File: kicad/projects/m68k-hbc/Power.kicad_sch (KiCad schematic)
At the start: 25 parts, among them J16 ATX-24

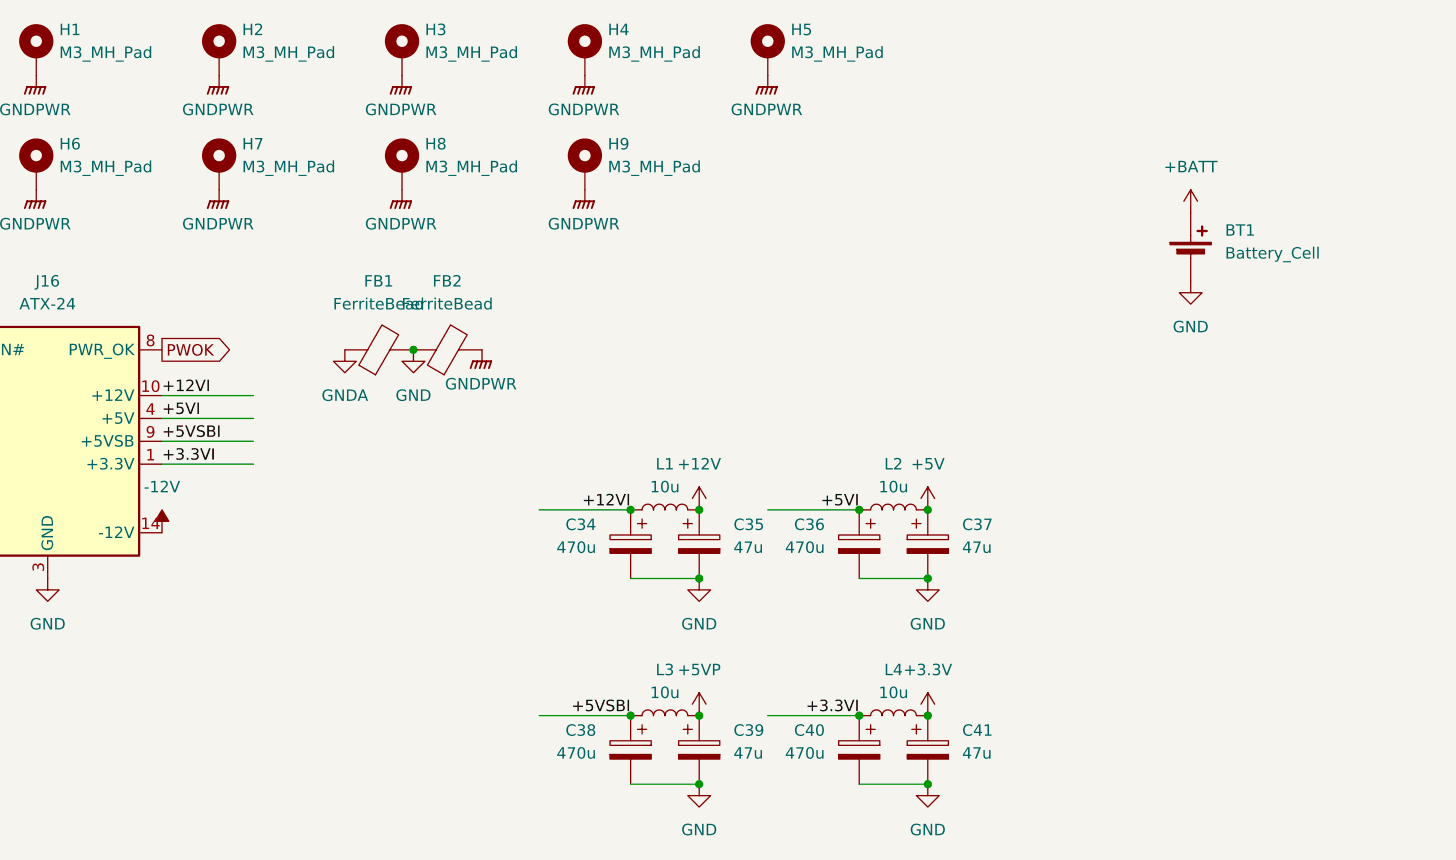
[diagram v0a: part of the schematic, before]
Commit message: Modified system architecture, New KiCad Project: Cache Memory Module(SIMM80)
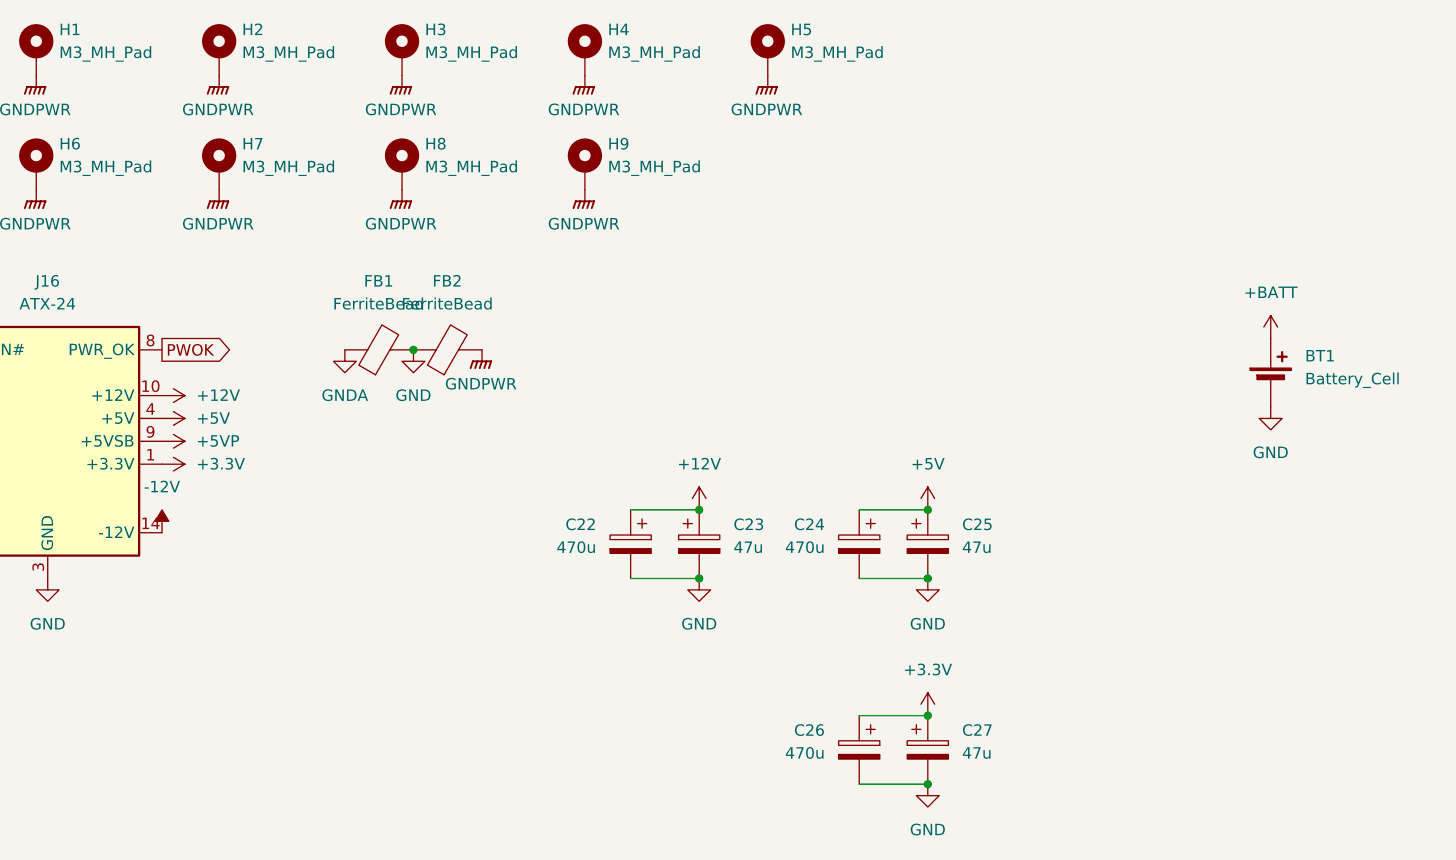
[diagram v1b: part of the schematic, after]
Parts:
- removed C38: 470u, Capacitor_THT:CP_Radial_D8.0mm_P3.50mm, symbol Device:C_Polarized
- removed C39: 47u, Capacitor_THT:CP_Radial_D8.0mm_P3.50mm, symbol Device:C_Polarized
- removed L1, L2, L3, L4: 10u, Inductor_THT:L_Toroid_Vertical_L13.0mm_W6.5mm_P5.60mm, symbol Device:L
- renumbered C34 to C22, C35 to C23, C36 to C24, C37 to C25, C40 to C26, C41 to C27
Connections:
- net +12VI is gone; now on net +12V: C22.1, J16.10 (+12V), J16.11 (+12V)
- net +3.3VI is gone; now on net +3.3V: C26.1, J16.1 (+3.3V), J16.12 (+3.3V), J16.13 (+3.3V), J16.2 (+3.3V)
- net +5VI is gone; now on net +5V: C24.1, J16.21 (+5V), J16.22 (+5V), J16.23 (+5V), J16.4 (+5V), J16.6 (+5V)
- net +5VSBI is gone; now on net +5VP: J16.9 (+5VSB)
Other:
- moved on the sheet: BT1

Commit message: Some Updates
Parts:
- added C132, C135, C136, C137, C138, C145, C146, C147, C148, C149, C150, C151, C154, C155, C156, C157, C158, C159, C160, C161, C162, C163, C164, C165: C, Capacitor_SMD:C_0603_1608Metric_Pad1.08x0.95mm_HandSolder, symbol Device:C
- added C133, C134, C143, C144: C_Polarized, Capacitor_THT:CP_Radial_D5.0mm_P2.50mm, symbol Device:C_Polarized
- added D2, D3, D4: D_Schottky, Diode_THT:D_5W_P12.70mm_Horizontal, symbol Device:D_Schottky
- added L8, L9: L, Inductor_SMD:L_10.4x10.4_H4.8, symbol Device:L
- added Q1, Q2: Q_PNP_BCE, RJK0651DPB-00:LFPAK_REN-M, symbol Device:Q_PNP_BCE
- added R40, R41, R42, R43, R44, R45, R46, R47, R48, R49, R50, R51, R52, R53, R54, R55, R56, R57, R58, R59, R60, R61, R62, R63: R, Resistor_SMD:R_0603_1608Metric_Pad0.98x0.95mm_HandSolder, symbol Device:R
- added RN5: R_Network08, Resistor_THT:R_Array_SIP9, symbol Device:R_Network08
- added U32: PAC1953x-x4MX, Package_DFN_QFN:VQFN-16-1EP_3x3mm_P0.5mm_EP1.1x1.1mm, symbol Sensor_Energy:PAC1953x-x4MX
- added U33, U34, U36, U37: RJK0651DPB-00-J5, LFPAK_REN, symbol RJK0651DPB-00:RJK0651DPB-00-J5
- added U35: LTC3886, Package_DFN_QFN:Linear_UGK52_QFN-46-52, symbol Regulator_Switching:LTC3886
- C139: renamed from C22; value 470u -> C_Polarized
- C140: renamed from C23; value 47u -> C_Polarized
- C141: renamed from C24; value 470u -> C_Polarized
- C142: renamed from C25; value 47u -> C_Polarized
- C152: renamed from C26; value 470u -> C_Polarized
- C153: renamed from C27; value 47u -> C_Polarized
- H1, H2, H3, H4, H5, H6, H7, H8, H9: value M3_MH_Pad -> MountingHole_Pad
- renumbered FB1 to FB2, FB2 to FB3
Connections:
- net +12V: now also C132.1, R40.2, R44.1, R45.1, U32.12 (SENSE1-), U33.5, U34.5, U35.47 (Iin+); no longer J16.10 (+12V), J16.11 (+12V)
- net +3.3V: now also R42.2, U32.7 (SENSE3-); no longer J16.1 (+3.3V), J16.12 (+3.3V), J16.13 (+3.3V), J16.2 (+3.3V)
- net +5V: now also R41.2, U32.14 (SENSE2-), U32.2 (V_{DD}); no longer J16.21 (+5V), J16.22 (+5V), J16.23 (+5V), J16.4 (+5V), J16.6 (+5V)
- net GND: now also C132.2, C133.2, C134.2, C135.2, C136.2, C137.2, C138.2, C143.2, C144.2, C145.2, C146.2, C147.2, C148.2, C149.1, C150.2, C151.2, C158.2, C159.2, C160.2, C161.2, C162.2, C163.2, C164.2, C165.2, D4.2 (A), Q1.1 (B), Q1.2 (C), Q2.1 (B), Q2.2 (C), R43.2, R58.2, R59.2, R60.2, R61.2, R62.2, U32.10 (GND), U32.17 (EP), U32.3 (GND), U32.9 (GND), U35.26 (PHAS_CFG), U35.28 (WP), U35.53 (GND), U35.8 (Vsense0-), U36.1, U36.2, U36.3, U37.1, U37.2, U37.3
- new net: C154.1, L8.2, U33.1, U33.2, U33.3, U35.1 (SW0), U36.5
- new net: C157.2, R51.1, U35.10 (Isense1-)
- new net: C160.1, U35.11 (Ithr0)
- new net: C161.1, U35.12 (Ith0)
- new net: U33.4, U35.2 (TG0)
- new net: C164.1, U35.31 (Ith1)
- new net: C165.1, U35.32 (Ithr1)
- new net: C159.1, Q2.3 (E), U35.36 (TSNS1)
- new net: U34.4, U35.38 (TG1)
- new net: C155.2, L9.1, U34.1, U34.2, U34.3, U35.39 (SW1), U37.5
- new net: C156.1, R48.2, U35.4 (Isense0+)
- new net: C155.1, D3.1 (K), U35.40 (BOOST1)
- new net: U35.42 (BG1), U37.4
- new net: R52.2, U35.43 (EXTVcc), U35.7 (Vsense0+)
- new net: C150.1, C151.1, D2.2 (A), D3.2 (A), U35.44 (INTVcc)
- new net: R45.2, U35.46 (Iin-)
- new net: C149.2, R44.2, U35.48 (Vin)
- new net: C156.2, R50.2, U35.5 (Isense0-)
- new net: U35.50 (BG0), U36.4
- new net: C154.2, D2.1 (K), U35.52 (BOOST0)
- new net: C158.1, Q1.3 (E), U35.6 (TSNS0)
- new net: C157.1, R49.1, U35.9 (Isense1+)
- new net: J16.10 (+12V), J16.11 (+12V), R40.1, U32.11 (SENSE1+)
- new net: J16.21 (+5V), J16.22 (+5V), J16.23 (+5V), J16.4 (+5V), J16.6 (+5V), R41.1, U32.13 (SENSE2+)
- new net: R43.1, U32.6 (ADDRSEL)
- new net: J16.1 (+3.3V), J16.12 (+3.3V), J16.13 (+3.3V), J16.2 (+3.3V), R42.1, U32.8 (SENSE3+)
- new net: L8.1, R46.2, R48.1
- new net: L9.2, R47.1, R49.2
- new net ASEL0: R56.2, R61.1, U35.21 (ASEL0)
- new net ASEL1: R57.2, R62.1, U35.22 (ASEL1)
- new net FREQ_CFG: R55.2, R60.1, U35.25 (FREQ_CFG)
- new net PGOOD0: RN5.5 (R4), U35.34 (PGOOD0)
- new net PGOOD1: RN5.6 (R5), U35.33 (PGOOD1)
- new net PWR_CPURAM: C133.1, C134.1, C135.1, C136.1, C137.1, C138.1
- new net PWR_FPGA: C143.1, C144.1, C145.1, C146.1, C147.1, C148.1, R47.2, R51.2, U35.35 (Vsense1+)
- new net PWR_PROCESSOR: D4.1 (K), R46.1, R50.1, R52.1
- new net RUN0: RN5.8 (R7), U35.19 (RUN0)
- new net RUN1: RN5.9 (R8), U35.20 (RUN1)
- new net SHARE_CLK: RN5.7 (R6), U35.29 (SHARE_CLK)
- new net SYNC: R63.2, U35.13 (SYNC)
- new net SYS_SCL: U32.4 (SCL)
- new net SYS_SDA: U32.5 (SDA)
- new net VDD25: C163.1, R53.1, R54.1, R55.1, R56.1, R57.1, U35.27 (Vdd25)
- new net VDD33: C162.1, R63.1, RN5.1 (common), U35.30 (Vdd33)
- new net VOUT_CFG0: R53.2, R58.1, U35.23 (Vout_cfg0)
- new net VOUT_CFG1: R54.2, R59.1, U35.24 (Vout_cfg1)
- new net ~{ALERT}: RN5.2 (R1), U35.16 (~{ALERT})
- new net ~{FAULT0}: RN5.3 (R2), U35.17 (~{FAULT0})
- new net ~{FAULT1}: RN5.4 (R3), U35.18 (~{FAULT1})
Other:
- note added: "+5V"
- note added: "System Serial Bus"
- moved on the sheet: BT1, C139, C140, C141, C142, C152, C153, FB2, FB3, H1, H2, H3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

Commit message: Large changes: EHBCSimpleEmu, kicad, fwcode, docs
This commit contains some large changes:
- Removed EHBCSimpleEmu (Moved to kms1212/llemu, kms1212/qemu)
- (likely) Removed fwcode; now it only boots and stops
- Modified documents
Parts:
- removed BT1: Battery_Cell, Battery:BatteryHolder_ComfortableElectronic_CH273-2450_1x2450, symbol Device:Battery_Cell
- removed C132, C135, C136, C137, C138, C145, C146, C147, C148, C149, C150, C151, C154, C155, C156, C157, C158, C159, C160, C161, C162, C163, C164, C165: C, Capacitor_SMD:C_0603_1608Metric_Pad1.08x0.95mm_HandSolder, symbol Device:C
- removed C133, C134, C143, C144: C_Polarized, Capacitor_THT:CP_Radial_D5.0mm_P2.50mm, symbol Device:C_Polarized
- removed C139, C140, C141, C142, C152, C153: C_Polarized, Capacitor_THT:CP_Radial_D8.0mm_P3.50mm, symbol Device:C_Polarized
- removed D2, D3, D4: D_Schottky, Diode_THT:D_5W_P12.70mm_Horizontal, symbol Device:D_Schottky
- removed FB2, FB3: FerriteBead, Inductor_THT:L_Axial_L5.0mm_D3.6mm_P10.00mm_Horizontal_Murata_BL01RN1A2A2, symbol Device:FerriteBead
- removed H1, H2, H3, H4, H5, H6, H7, H8, H9: MountingHole_Pad, MountingHole:MountingHole_3.2mm_M3_Pad, symbol Mechanical:MountingHole_Pad
- removed J16: ATX-24, Connector_Molex:Molex_Mini-Fit_Jr_5566-24A_2x12_P4.20mm_Vertical, symbol Connector:ATX-24
- removed L8, L9: L, Inductor_SMD:L_10.4x10.4_H4.8, symbol Device:L
- removed Q1, Q2: Q_PNP_BCE, RJK0651DPB-00:LFPAK_REN-M, symbol Device:Q_PNP_BCE
- removed R40, R41, R42, R43, R44, R45, R46, R47, R48, R49, R50, R51, R52, R53, R54, R55, R56, R57, R58, R59, R60, R61, R62, R63: R, Resistor_SMD:R_0603_1608Metric_Pad0.98x0.95mm_HandSolder, symbol Device:R
- removed RN5: R_Network08, Resistor_THT:R_Array_SIP9, symbol Device:R_Network08
- removed U32: PAC1953x-x4MX, Package_DFN_QFN:VQFN-16-1EP_3x3mm_P0.5mm_EP1.1x1.1mm, symbol Sensor_Energy:PAC1953x-x4MX
- removed U33, U34, U36, U37: RJK0651DPB-00-J5, LFPAK_REN, symbol RJK0651DPB-00:RJK0651DPB-00-J5
- removed U35: LTC3886, Package_DFN_QFN:Linear_UGK52_QFN-46-52, symbol Regulator_Switching:LTC3886
- added J12: ATX-24, Connector_Molex:Molex_Mini-Fit_Jr_5566-24A_2x12_P4.20mm_Vertical, symbol Connector:ATX-24
- added U15: SYS_Header, Connector_PinHeader_2.54mm:PinHeader_2x08_P2.54mm_Vertical, symbol m68k-hbc-conn:SYS_Header
- added U20: ADP5050ACPZ, Package_CSP:LFCSP-48-1EP_7x7mm_P0.5mm_EP4.1x4.1mm_ThermalVias, symbol m68k-hbc-ic:ADP5050ACPZ
- added U21: PAC1932x-xJQ, Package_DFN_QFN:UQFN-16-1EP_4x4mm_P0.65mm_EP2.6x2.6mm, symbol Sensor_Energy:PAC1932x-xJQ
- added U23: STM6601, Package_DFN_QFN:TDFN-12_2x3mm_P0.5mm, symbol Power_Management:STM6601
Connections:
- net +12V: now also J12.10 (+12V), J12.11 (+12V)
- net +3.3V: now also J12.1 (+3.3V), J12.12 (+3.3V), J12.13 (+3.3V), J12.2 (+3.3V)
- net +5V: now also J12.21 (+5V), J12.22 (+5V), J12.23 (+5V), J12.4 (+5V), J12.6 (+5V)
- net -12V: now also J12.14 (-12V)
- net GND: now also J12.15 (GND), J12.17 (GND), J12.18 (GND), J12.19 (GND), J12.24 (GND), J12.3 (GND), J12.5 (GND), J12.7 (GND), U15.11 (HDD-), U15.12 (RSW-), U15.15 (PWR-), U15.16 (PSW-), U15.2 (GND), U15.6 (GND), U15.7 (BUZ-), U23.12 (GND)
- new net: U21.10 (GND), U21.3 (GND), U21.7 (GND), U21.8 (GND), U21.9 (GND)
- new net +5VSB: J12.9 (+5VSB), U23.1 (Vcc)
- new net PWR+: U15.14 (PSW+), U23.6 (~{PB})
- new net RST+: U15.10 (RSW+), U23.2 (~{SR})
- new net ~{BTN_INT}: U23.11 (~{INT})
- new net ~{BTN_OUT}: U23.8 (~{PB}_OUT)
- new net ~{BUCK_INT}: U20.13 (~{INT})
- new net ~{RST}: U23.10 (~{RST})
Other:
- note removed: "+5V"
- note removed: "System Serial Bus"
